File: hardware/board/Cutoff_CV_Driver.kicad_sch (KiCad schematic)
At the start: 18 parts

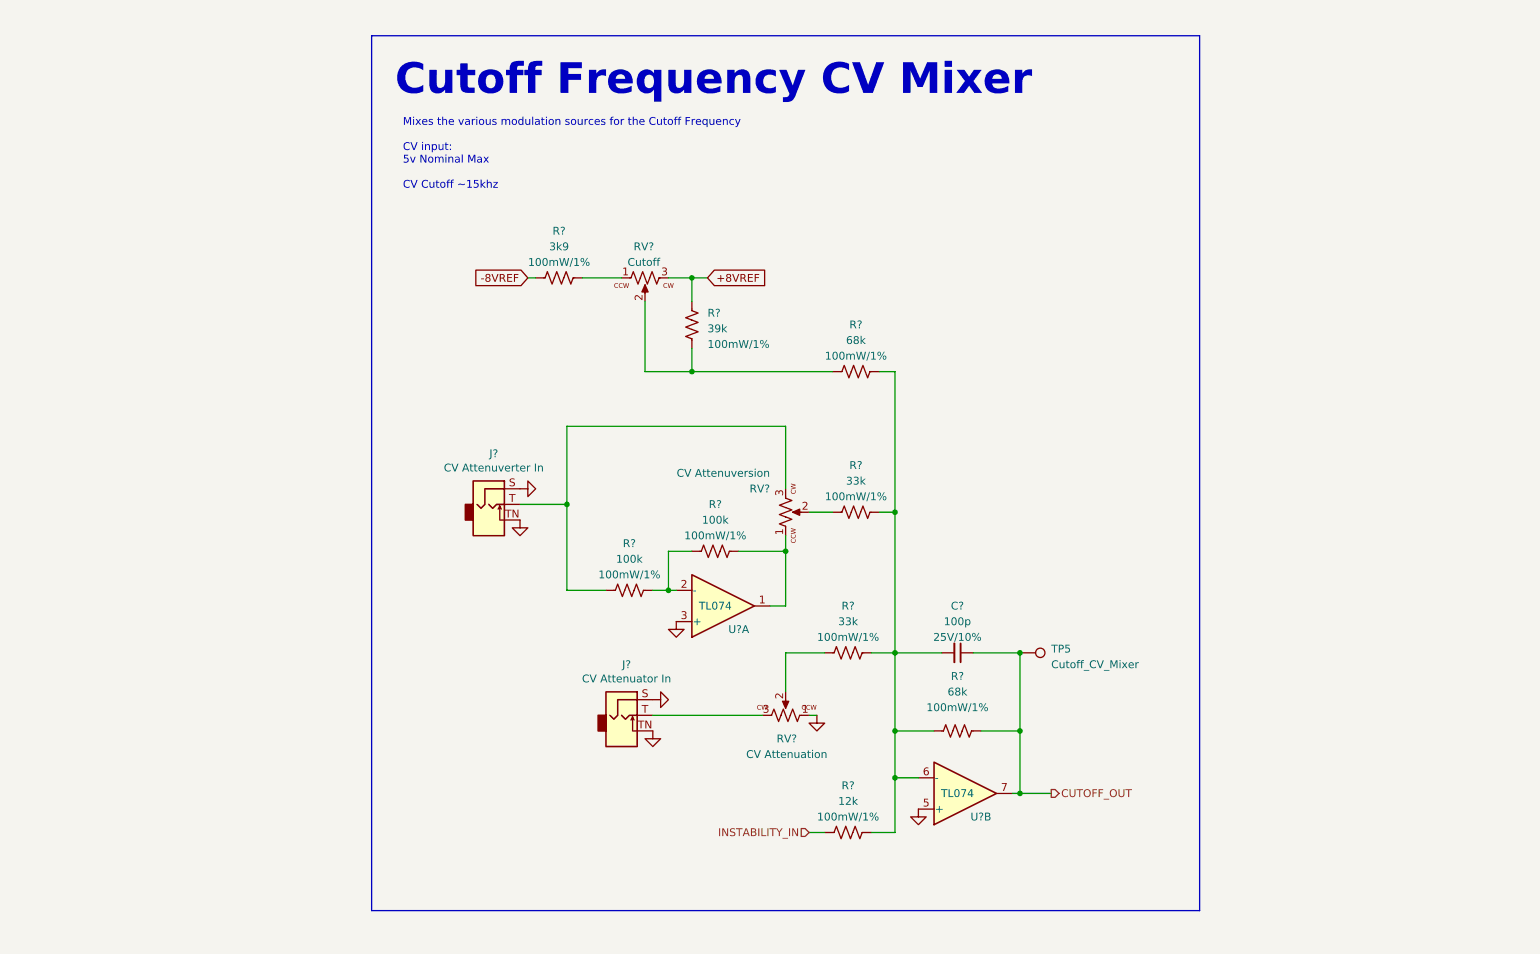
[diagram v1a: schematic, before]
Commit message: BOM Consolidation
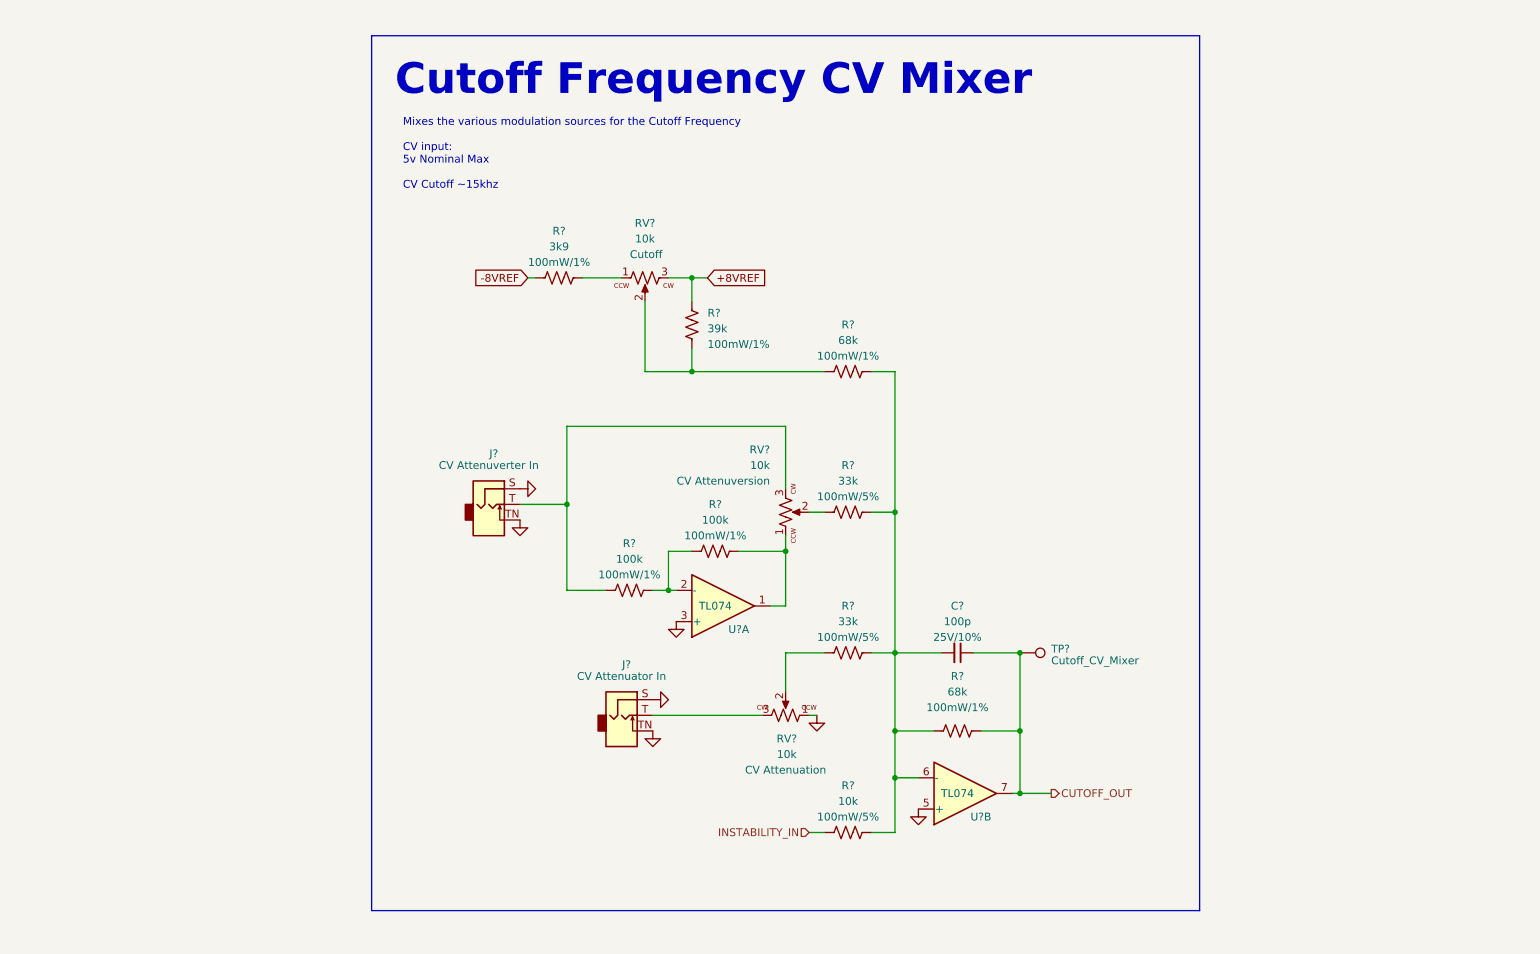
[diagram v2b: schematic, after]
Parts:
- J?: value CV Attenuverter In -> ~; Name (none) -> CV Attenuverter In
- J?: value CV Attenuator In -> ~; Name (none) -> CV Attenuator In
- R?: value 12k -> 10k; Rating 100mW/1% -> 100mW/5%
- R? (x2): Rating 100mW/1% -> 100mW/5%
- RV?: value Cutoff -> 10k; Name (none) -> Cutoff
- RV?: value CV Attenuation -> 10k; Name (none) -> CV Attenuation
- RV?: value CV Attenuversion -> 10k; Name (none) -> CV Attenuversion
- TP?: renamed from TP5; value Cutoff_CV_Mixer -> ~; Name (none) -> Cutoff_CV_Mixer
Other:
- moved on the sheet: R?
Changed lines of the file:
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@@
     (stroke (width 0) (type default))
   )
-  (wire (pts (xy 146.05 97.79) (xy 149.86 97.79))
-    (stroke (width 0) (type default))
-  )
-  (wire (pts (xy 157.48 97.79) (xy 160.02 97.79))
+  (wire (pts (xy 146.05 97.79) (xy 148.59 97.79))
+    (stroke (width 0) (type default))
+  )
+  (wire (pts (xy 156.21 97.79) (xy 160.02 97.79))
     (stroke (width 0) (type default))
   )
@@
     (stroke (width 0) (type default))
   )
-  (wire (pts (xy 127 74.93) (xy 149.86 74.93))
+  (wire (pts (xy 127 74.93) (xy 148.59 74.93))
     (stroke (width 0) (type default))
   )
@@
     (stroke (width 0) (type default))
   )
-  (wire (pts (xy 160.02 74.93) (xy 157.48 74.93))
+  (wire (pts (xy 160.02 74.93) (xy 156.21 74.93))
     (stroke (width 0) (type default))
   )
@@
   (symbol (lib_id "winterbloom:Eurorack_Pot") (at 119.38 59.69 0) (unit 1)
     (in_bom yes) (on_board yes) (dnp no)
-    (property "Reference" "RV?" (at 119.1896 54.61 0)
-      (effects (font (size 1.27 1.27)))
-    )
-    (property "Value" "Cutoff" (at 119.1896 57.15 0)
+    (property "Reference" "RV?" (at 119.38 50.8 0)
+      (effects (font (size 1.27 1.27)))
+    )
+    (property "Value" "10k" (at 119.38 53.34 0)
       (effects (font (size 1.27 1.27)))
     )
@@
     (property "Rating" "B10k" (at 119.38 59.69 0)
       (effects (font (size 1.27 1.27)) hide)
+    )
+    (property "Name" "Cutoff" (at 119.5704 55.88 0)
+      (effects (font (size 1.27 1.27)))
     )
     (pin "1")
@@
   )
   (symbol (lib_id "Connector:TestPoint") (at 180.34 120.65 270) (unit 1)
-    (in_bom yes) (on_board yes) (dnp no) (fields_autoplaced)
-    (property "Reference" "TP5" (at 185.42 120.015 90)
+    (in_bom yes) (on_board yes) (dnp no)
+    (property "Reference" "TP?" (at 185.42 120.015 90)
       (effects (font (size 1.27 1.27)) (justify left))
     )
-    (property "Value" "Cutoff_CV_Mixer" (at 185.42 122.555 90)
+    (property "Value" "~" (at 185.42 122.555 90)
       (effects (font (size 1.27 1.27)) (justify left))
     )
@@
       (effects (font (size 1.27 1.27)) hide)
     )
+    (property "Name" "Cutoff_CV_Mixer" (at 185.42 121.92 90)
+      (effects (font (size 1.27 1.27)) (justify left))
+    )
     (pin "1")
     (instances
       (project "mainboard"
         (path "/960bd036-bf0c-45ea-9f41-1321756e0e5a/48d891c0-35ba-4c8e-a930-c990a10298eb"
-          (reference "TP5") (unit 1)
-        )
-        (path "/960bd036-bf0c-45ea-9f41-1321756e0e5a/193c5b93-4c44-4f6f-9ef0-5f8993e4582d"
-          (reference "TP13") (unit 1)
+          (reference "TP?") (unit 1)
+        )
+        (path "/960bd036-bf0c-45ea-9f41-1321756e0e5a/193c5b93-4c44-4f6f-9ef0-5f8993e4582d"
+          (reference "TP?") (unit 1)
         )
       )
@@
       (effects (font (size 1.27 1.27)))
     )
-    (property "Value" "12k" (at 152.4 144.78 90)
+    (property "Value" "10k" (at 152.4 144.78 90)
       (effects (font (size 1.27 1.27)))
     )
@@
       (effects (font (size 1.27 1.27)) hide)
     )
-    (property "Rating" "100mW/1%" (at 152.4 147.32 90)
+    (property "Rating" "100mW/5%" (at 152.4 147.32 90)
       (effects (font (size 1.27 1.27)))
     )
@@
     )
   )
-  (symbol (lib_id "Device:R_US") (at 153.67 97.79 270) (unit 1)
-    (in_bom yes) (on_board yes) (dnp no) (fields_autoplaced)
-    (property "Reference" "R?" (at 153.67 90.17 90)
-      (effects (font (size 1.27 1.27)))
-    )
-    (property "Value" "33k" (at 153.67 92.71 90)
-      (effects (font (size 1.27 1.27)))
-    )
-    (property "Footprint" "winterbloom:R_0603_HandSolder" (at 153.416 98.806 90)
-      (effects (font (size 1.27 1.27)) hide)
-    )
-    (property "Datasheet" "~" (at 153.67 97.79 0)
-      (effects (font (size 1.27 1.27)) hide)
-    )
-    (property "mpn" "" (at 153.67 97.79 0)
-      (effects (font (size 1.27 1.27)) hide)
-    )
-    (property "Notes" "" (at 153.67 97.79 0)
-      (effects (font (size 1.27 1.27)) hide)
-    )
-    (property "smd kit" "1" (at 153.67 97.79 0)
-      (effects (font (size 1.27 1.27)) hide)
-    )
-    (property "Rating" "100mW/1%" (at 153.67 95.25 90)
+  (symbol (lib_id "Device:R_US") (at 152.4 97.79 270) (unit 1)
+    (in_bom yes) (on_board yes) (dnp no) (fields_autoplaced)
+    (property "Reference" "R?" (at 152.4 90.17 90)
+      (effects (font (size 1.27 1.27)))
+    )
+    (property "Value" "33k" (at 152.4 92.71 90)
+      (effects (font (size 1.27 1.27)))
+    )
+    (property "Footprint" "winterbloom:R_0603_HandSolder" (at 152.146 98.806 90)
+      (effects (font (size 1.27 1.27)) hide)
+    )
+    (property "Datasheet" "~" (at 152.4 97.79 0)
+      (effects (font (size 1.27 1.27)) hide)
+    )
+    (property "mpn" "" (at 152.4 97.79 0)
+      (effects (font (size 1.27 1.27)) hide)
+    )
+    (property "Notes" "" (at 152.4 97.79 0)
+      (effects (font (size 1.27 1.27)) hide)
+    )
+    (property "smd kit" "1" (at 152.4 97.79 0)
+      (effects (font (size 1.27 1.27)) hide)
+    )
+    (property "Rating" "100mW/5%" (at 152.4 95.25 90)
       (effects (font (size 1.27 1.27)))
     )
@@
       (effects (font (size 1.27 1.27)))
     )
-    (property "Value" "CV Attenuverter In" (at 94.7928 90.5764 0)
+    (property "Value" "~" (at 94.7928 90.5764 0)
       (effects (font (size 1.27 1.27)))
     )
@@
     (property "MPN" "WQP-WQP518MA" (at 93.98 91.44 0)
       (effects (font (size 1.27 1.27)) hide)
+    )
+    (property "Name" "CV Attenuverter In" (at 93.98 90.17 0)
+      (effects (font (size 1.27 1.27)))
     )
     (pin "S")
@@
       (effects (font (size 1.27 1.27)))
     )
-    (property "Value" "CV Attenuation" (at 142.4305 137.16 0)
+    (property "Value" "10k" (at 142.4305 137.16 0)
       (effects (font (size 1.27 1.27)))
     )
@@
     (property "Rating" "B10k" (at 142.24 130.81 0)
       (effects (font (size 1.27 1.27)) hide)
+    )
+    (property "Name" "CV Attenuation" (at 142.24 139.7 0)
+      (effects (font (size 1.27 1.27)))
     )
     (pin "1")
@@
       (effects (font (size 1.27 1.27)) hide)
     )
-    (property "Rating" "100mW/1%" (at 152.4 118.11 90)
+    (property "Rating" "100mW/5%" (at 152.4 118.11 90)
       (effects (font (size 1.27 1.27)))
     )
@@
       (effects (font (size 1.27 1.27)))
     )
-    (property "Value" "CV Attenuator In" (at 116.3828 124.8664 0)
+    (property "Value" "~" (at 116.3828 124.8664 0)
       (effects (font (size 1.27 1.27)))
     )
@@
     (property "MPN" "WQP-WQP518MA" (at 115.57 125.73 0)
       (effects (font (size 1.27 1.27)) hide)
+    )
+    (property "Name" "CV Attenuator In" (at 115.57 124.46 0)
+      (effects (font (size 1.27 1.27)))
     )
     (pin "S")
@@
   (symbol (lib_id "winterbloom:Eurorack_Pot") (at 142.24 97.79 90) (unit 1)
     (in_bom yes) (on_board yes) (dnp no)
-    (property "Reference" "RV?" (at 139.7 93.98 90)
+    (property "Reference" "RV?" (at 139.7 87.63 90)
       (effects (font (size 1.27 1.27)) (justify left))
     )
-    (property "Value" "CV Attenuversion" (at 139.7 91.44 90)
+    (property "Value" "10k" (at 139.7 90.17 90)
       (effects (font (size 1.27 1.27)) (justify left))
     )
@@
     (property "Rating" "B10k" (at 142.24 97.79 0)
       (effects (font (size 1.27 1.27)) hide)
+    )
+    (property "Name" "CV Attenuversion" (at 139.7 92.71 90)
+      (effects (font (size 1.27 1.27)) (justify left))
     )
     (pin "1")
@@
     )
   )
-  (symbol (lib_id "Device:R_US") (at 153.67 74.93 90) (unit 1)
+  (symbol (lib_id "Device:R_US") (at 152.4 74.93 90) (unit 1)
     (in_bom yes) (on_board yes) (dnp no)
-    (property "Reference" "R?" (at 153.67 67.31 90)
-      (effects (font (size 1.27 1.27)))
-    )
-    (property "Value" "68k" (at 153.67 69.85 90)
-      (effects (font (size 1.27 1.27)))
-    )
-    (property "Footprint" "winterbloom:R_0603_HandSolder" (at 153.924 73.914 90)
-      (effects (font (size 1.27 1.27)) hide)
-    )
-    (property "Datasheet" "~" (at 153.67 74.93 0)
-      (effects (font (size 1.27 1.27)) hide)
-    )
-    (property "mpn" "" (at 153.67 74.93 0)
-      (effects (font (size 1.27 1.27)) hide)
-    )
-    (property "Notes" "" (at 153.67 74.93 0)
-      (effects (font (size 1.27 1.27)) hide)
-    )
-    (property "smd kit" "1" (at 153.67 74.93 0)
-      (effects (font (size 1.27 1.27)) hide)
-    )
-    (property "Rating" "100mW/1%" (at 153.67 72.39 90)
-      (effects (font (size 1.27 1.27)))
-    )
+    (property "Reference" "R?" (at 152.4 67.31 90)
+      (effects (font (size 1.27 1.27)))
+    )
+    (property "Value" "68k" (at 152.4 69.85 90)
+      (effects (font (size 1.27 1.27)))
+    )
+    (property "Footprint" "winterbloom:R_0603_HandSolder" (at 152.654 73.914 90)
+      (effects (font (size 1.27 1.27)) hide)
+    )
+    (property "Datasheet" "~" (at 152.4 74.93 0)
+      (effects (font (size 1.27 1.27)) hide)
+    )
+    (property "mpn" "" (at 152.4 74.93 0)
+      (effects (font (size 1.27 1.27)) hide)
+    )
+    (property "Notes" "" (at 152.4 74.93 0)
+      (effects (font (size 1.27 1.27)) hide)
+    )
+    (property "smd kit" "1" (at 152.4 74.93 0)
+      (effects (font (size 1.27 1.27)) hide)
+    )
+    (property "Rating" "100mW/1%" (at 152.4 72.39 90)
+      (effects (font (size 1.27 1.27)))
+    )

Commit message: Updates for LED Drivers
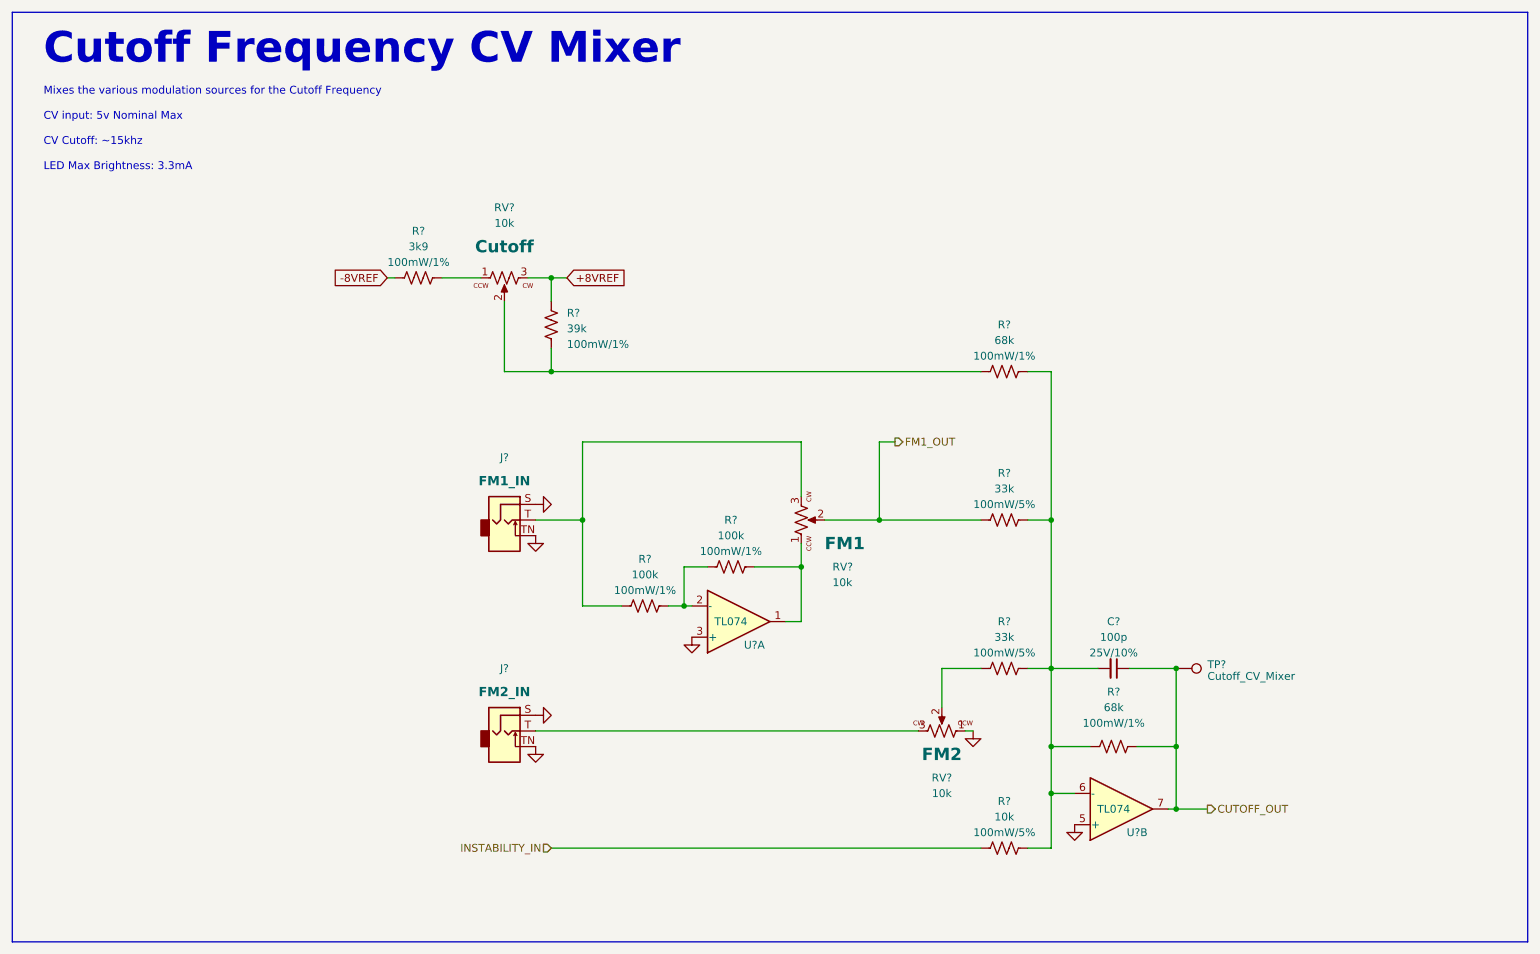
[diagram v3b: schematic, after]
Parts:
- J?: Name CV Attenuverter In -> FM1_IN
- J?: Name CV Attenuator In -> FM2_IN
- RV?: Name CV Attenuation -> FM2
- RV?: Name CV Attenuversion -> FM1
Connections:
- net FM1_OUT: now reaches R?.2, RV?.2
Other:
- note added: "Mixes the various modulation sources for the Cutoff Frequency CV input: 5v Nominal Max CV Cutoff: ~15khz LED Max Brightness: 3.3mA"
- note removed: "Mixes the various modulation sources for the Cutoff Frequency CV input: 5v Nominal Max CV Cutoff ~15khz"
- moved on the sheet: C?, J?, R?, RV?, TP?, U?A, U?B

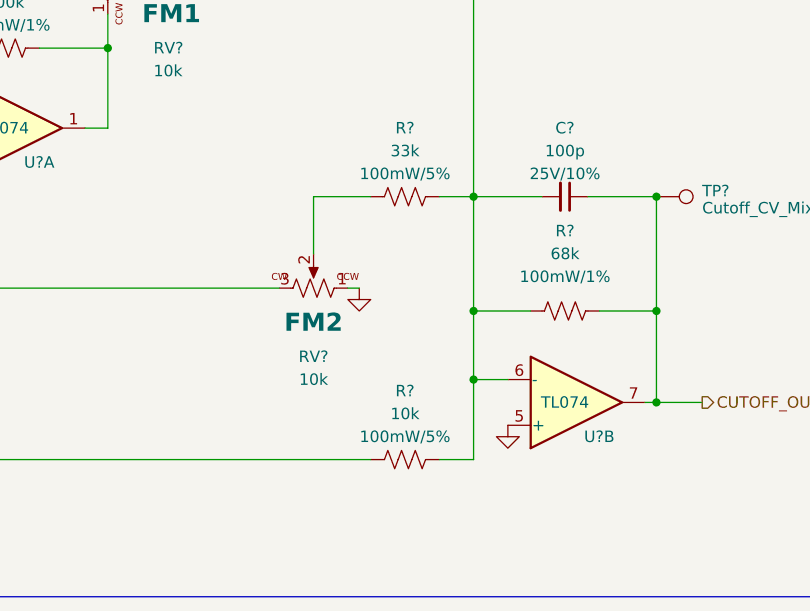
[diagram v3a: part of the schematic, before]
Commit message: hardware: update schematic with footprints and preliminary MPNs
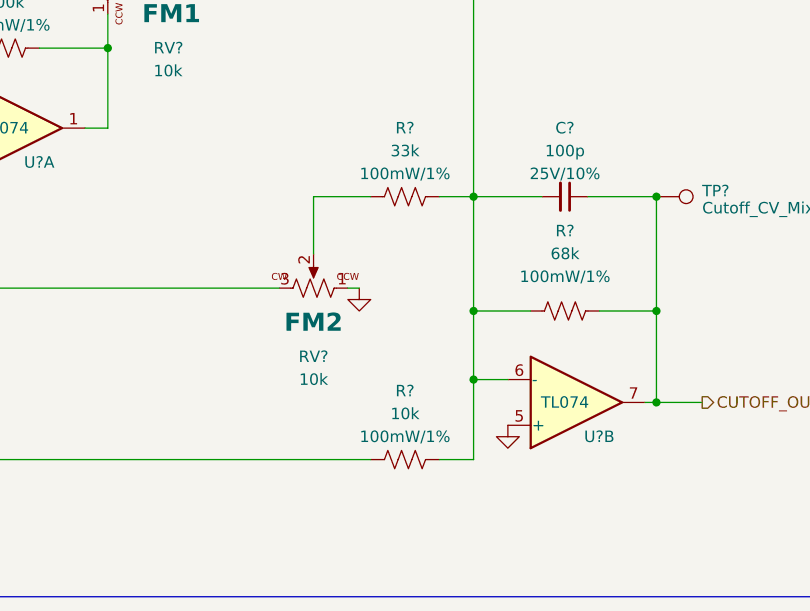
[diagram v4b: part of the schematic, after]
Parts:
- C?: Notes 0603, 25V+, 10% -> (none); smd kit 1 -> (none)
- J? (x2): mpn WQP-WQP518MA -> (none)
- R? (x7): smd kit 1 -> (none)
- R? (x2): Rating 100mW/5% -> 100mW/1%; smd kit 1 -> (none)
- TP?: footprint (none) -> TestPoint:TestPoint_Pad_D1.5mm
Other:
- title: Diode Ladder Filter -> Neptune

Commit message: Very first component layout.
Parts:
- removed U?: TL074, Package_SO:TSSOP-14_4.4x5mm_P0.65mm, symbol winterbloom:TL074
- added U?: TL074, Package_SO:TSSOP-14_4.4x5mm_P0.65mm, symbol winterbloom:TL074
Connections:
- net GND: now also U?.10 (+)
- net at R?.1, R?.2: now also U?.9 (-)
- net at R?.1, RV?.1: now also U?.8
